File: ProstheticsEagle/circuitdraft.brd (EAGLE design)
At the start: 60 x 29.8 mm, 49 parts, among them IC1 BQ25887RGER, IC2 TPS54627DDAR, Q1 16 MHz

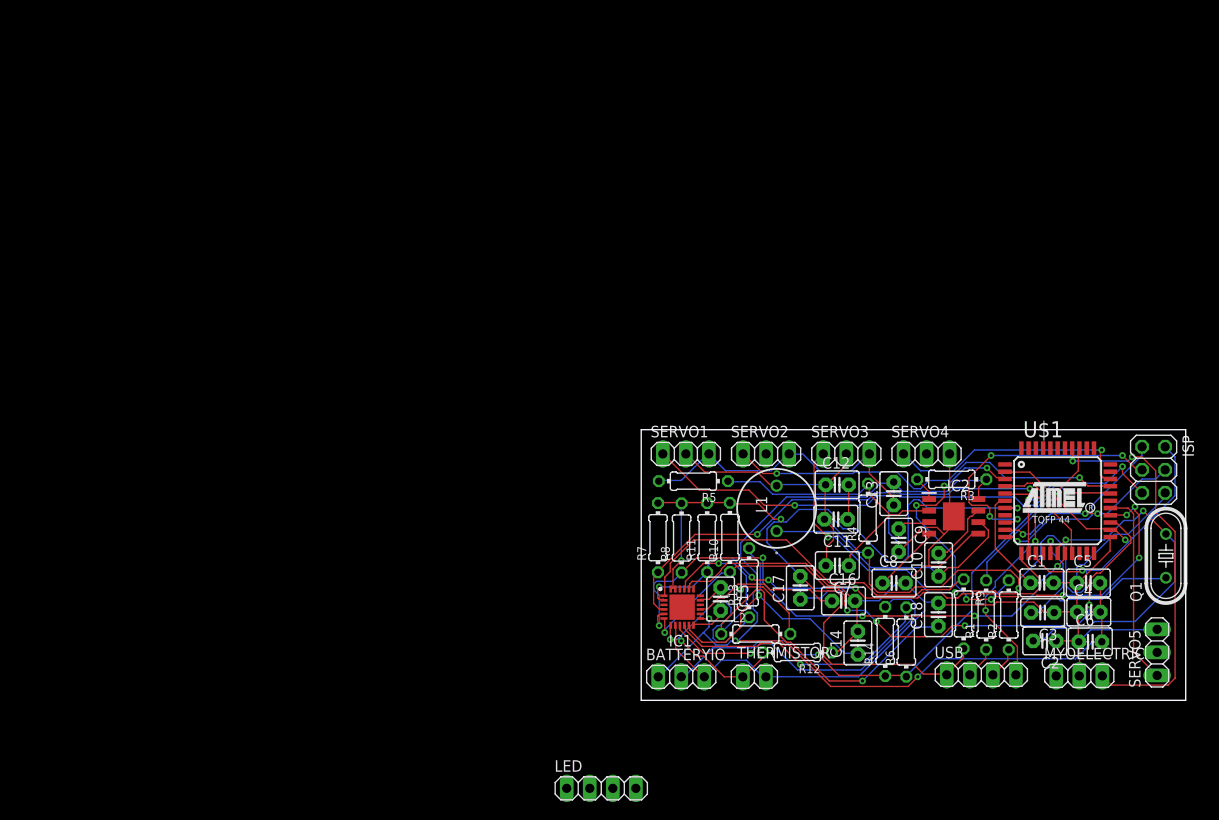
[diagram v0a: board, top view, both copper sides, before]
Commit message: Added surface mount parts
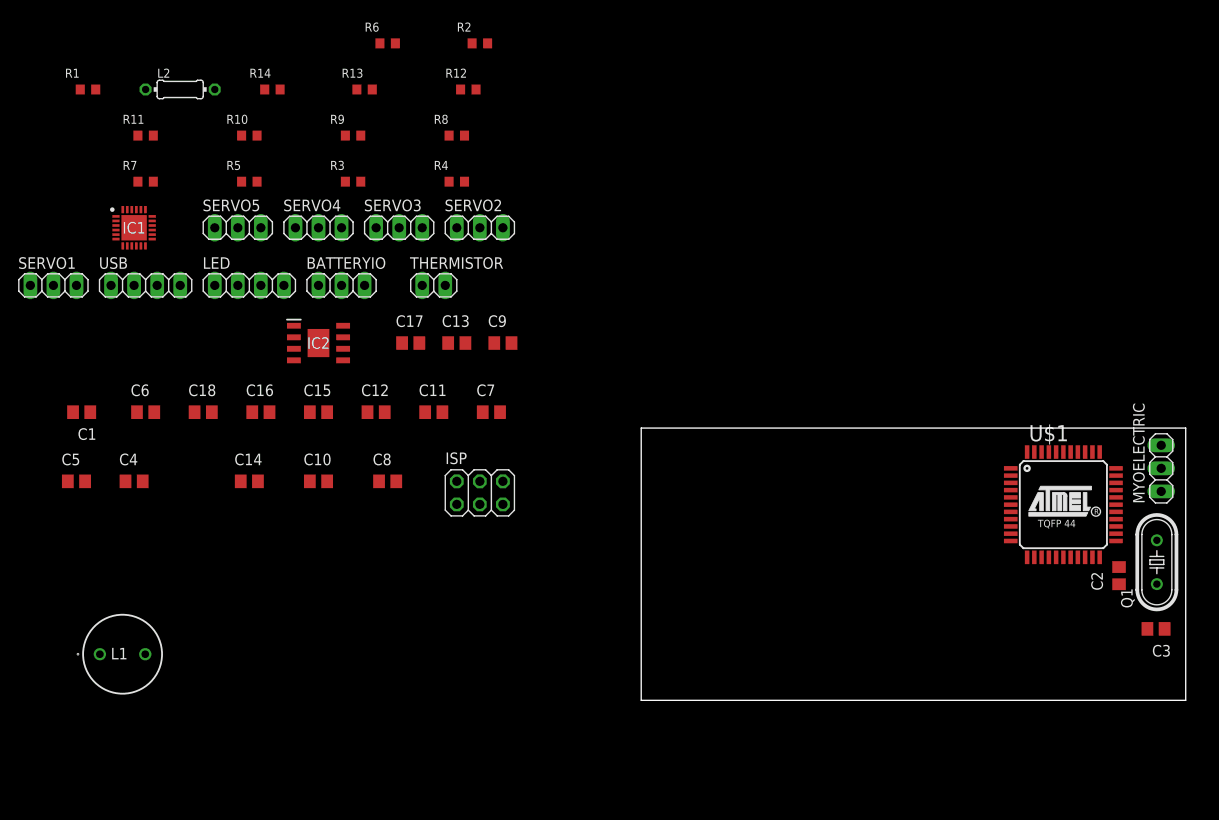
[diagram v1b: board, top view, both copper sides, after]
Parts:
- C1, C10, C11, C12, C13, C14, C15, C16, C17, C18, C2, C3, C4, C5, C6, C7, C8, C9: device capacitor-wima:C2.5-3 -> rcl:C0805
- R1, R10, R11, R12, R13, R14, R2, R3, R4, R5, R6, R7, R8, R9: device rcl:0204/7 -> rcl:R0603
- moved R1 114.7 mm to (-61.0, 67.3), turned to 0 degrees
- moved C5 112.1 mm to (-62.2, 24.1)
- moved SERVO5 111.6 mm to (-44.5, 52.1), turned to 0 degrees
- moved C1 107.5 mm to (-61.7, 31.8), turned to 180 degrees
- moved C6 107.1 mm to (-54.6, 31.8)
- moved C4 106.2 mm to (-55.9, 24.1)
- moved USB 101.6 mm to (-54.6, 45.7)
- moved R14 90.9 mm to (-40.6, 67.3), turned to 0 degrees
- moved L2 87.3 mm to (-50.8, 67.3)
- moved R6 87.3 mm to (-27.9, 72.4), turned to 0 degrees
- moved R2 85.8 mm to (-17.8, 72.4), turned to 0 degrees
- moved R9 85.5 mm to (-31.8, 62.2), turned to 0 degrees
- moved C18 84.0 mm to (-48.3, 31.8), turned to 0 degrees
- moved R11 76.1 mm to (-54.6, 62.2), turned to 0 degrees
- moved ISP 74.3 mm to (-17.8, 22.9), turned to 0 degrees
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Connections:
- removed net N$17: C11.1, C12.2
- removed net VOUT: MYOELECTRIC.1
- net AGND: now also C11.2, C12.2
- net POWER: now also C11.1, MYOELECTRIC.1; no longer C11.2
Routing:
- net AGND: track 216.7 -> 0.00 mm
- net POWER: track 121.4 -> 0.00 mm, vias 3 -> 0
- net B+: track 111.6 -> 0.00 mm, vias 3 -> 0
- net VBUS: track 101.7 -> 0.00 mm, vias 3 -> 0
- net INT: track 70.2 -> 0.00 mm, vias 5 -> 0
- net STAT: track 70.0 -> 0.00 mm, vias 8 -> 0
- net MIDDLE: track 61.5 -> 0.00 mm, vias 2 -> 0
- net SCL: track 61.1 -> 0.00 mm, vias 5 -> 0
- net SDA: track 59.1 -> 0.00 mm, vias 2 -> 0
- net SIGNAL1: track 53.8 -> 0.00 mm, vias 2 -> 0
- net N$21: track 51.7 -> 0.00 mm, vias 2 -> 0
- net SIGNAL2: track 44.5 -> 0.00 mm, vias 2 -> 0
- net N$12: track 43.9 -> 0.00 mm, vias 2 -> 0
- net SIGNAL3: track 41.3 -> 0.00 mm, vias 2 -> 0
- net N$7: track 40.5 -> 0.00 mm
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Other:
- board size 60 x 29.8 mm -> 60 x 30 mm

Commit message: fffff
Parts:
- removed BATTERYIO, MYOELECTRIC: (no value), pinhead:1X03
- removed THERMISTOR: (no value), pinhead:1X02
- added BATIO, MYO: (no value), pinhead:1X03
- added TS: (no value), pinhead:1X02
- LED: device pinhead:1X04 -> pinhead:1X03
- moved R7 112.0 mm to (48.9, 14.4)
- moved SERVO5 111.7 mm to (55.6, 2.57)
- moved R1 95.5 mm to (24.7, 25.0)
- moved R11 91.4 mm to (21.9, 12.1)
- moved C1 85.9 mm to (22.4, 14.2)
- moved R14 80.5 mm to (11.4, 5.91)
- moved R10 80.4 mm to (22.5, 15.9)
- moved L2 80.0 mm to (5.50, 10.4)
- moved C5 78.5 mm to (15.9, 16.4)
- moved R6 77.5 mm to (15.4, 8.09)
- moved IC1 77.0 mm to (11.0, 13.9), turned to 90 degrees
- moved R5 76.5 mm to (22.5, 18.1)
- moved R9 75.6 mm to (18.6, 5.93)
- moved C6 73.1 mm to (15.8, 12.2)
- moved C4 72.4 mm to (15.8, 14.3)
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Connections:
- removed net N$12: MYOELECTRIC.3, U$1.37
- removed net N$23: LED.4
- removed net N$24: LED.1
- new net DATAIN: LED.3
- new net MYOSIGNAL: MYO.3, U$1.37
- net AGND: now also BATIO.3, LED.2, MYO.2, TS.2; no longer BATTERYIO.3, LED.3, MYOELECTRIC.2, THERMISTOR.2
- net B+: now also BATIO.1; no longer BATTERYIO.1
- net MIDDLE: now also BATIO.2; no longer BATTERYIO.2
- net POWER: now also LED.1, MYO.1, SERVO2.2, SERVO4.2, SERVO5.2; no longer LED.2, MYOELECTRIC.1
- net TS: now also TS.1; no longer THERMISTOR.1
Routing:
- added copper zone on layer 1, net AGND
- added copper zone on layer 16, net AGND

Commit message: moved stuff
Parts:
- moved R10 3.32 mm to (25.8, 16.3)
- moved R6 0.41 mm to (15.8, 7.99)
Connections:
- net DATAIN: now also U$1.32
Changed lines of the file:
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@@
 </class>
 </classes>
-<designrules name="default">
-<description language="de">&lt;b&gt;EAGLE Design Rules&lt;/b&gt;
+<designrules name="jlcpcb2layer">
+<description language="en">&lt;b&gt;JLCPCB Design Rules by Jaap de Dood&lt;/b&gt;
 &lt;p&gt;
-Die Standard-Design-Rules sind so gewählt, dass sie für
-die meisten Anwendungen passen. Sollte ihre Platine
-besondere Anforderungen haben, treffen Sie die erforderlichen
-Einstellungen hier und speichern die Design Rules unter
-einem neuen Namen ab.</description>
-<description language="en">&lt;b&gt;EAGLE Design Rules&lt;/b&gt;
-&lt;p&gt;
-The default Design Rules have been set to cover
-a wide range of applications. Your particular design
-may have different requirements, so please make the
-necessary adjustments and save your customized
-design rules under a new name.</description>
+Please make sure your boards conform to these design rules.
+&lt;/p&gt;</description>
 <param name="layerSetup" value="(1*16)"/>
-<param name="mtCopper" value="0.035mm 0.035mm 0.035mm 0.035mm 0.035mm 0.035mm 0.035mm 0.035mm 0.035mm 0.035mm 0.035mm 0.035mm 0.035mm 0.035mm 0.035mm 0.035mm"/>
-<param name="mtIsolate" value="1.5mm 0.15mm 0.2mm 0.15mm 0.2mm 0.15mm 0.2mm 0.15mm 0.2mm 0.15mm 0.2mm 0.15mm 0.2mm 0.15mm 0.2mm"/>
-<param name="mdWireWire" value="6mil"/>
-<param name="mdWirePad" value="6mil"/>
-<param name="mdWireVia" value="6mil"/>
-<param name="mdPadPad" value="6mil"/>
-<param name="mdPadVia" value="6mil"/>
-<param name="mdViaVia" value="6mil"/>
-<param name="mdSmdPad" value="6mil"/>
-<param name="mdSmdVia" value="6mil"/>
-<param name="mdSmdSmd" value="6mil"/>
-<param name="mdViaViaSameLayer" value="6mil"/>
+<param name="mtCopper" value="0.035559375mm 0.0356mm 0.0356mm 0.0356mm 0.0356mm 0.0356mm 0.0356mm 0.0356mm 0.0356mm 0.0356mm 0.0356mm 0.0356mm 0.0356mm 0.0356mm 0.0356mm 0.035559375mm"/>
+<param name="mtIsolate" value="1.6mm 0.1499mm 0.2007mm 0.1499mm 0.2007mm 0.1499mm 0.2007mm 0.1499mm 0.2007mm 0.1499mm 0.2007mm 0.1499mm 0.2007mm 0.1499mm 0.2007mm"/>
+<param name="mdWireWire" value="5mil"/>
+<param name="mdWirePad" value="5mil"/>
+<param name="mdWireVia" value="5mil"/>
+<param name="mdPadPad" value="5mil"/>
+<param name="mdPadVia" value="5mil"/>
+<param name="mdViaVia" value="5mil"/>
+<param name="mdSmdPad" value="5mil"/>
+<param name="mdSmdVia" value="5mil"/>
+<param name="mdSmdSmd" value="5mil"/>
+<param name="mdViaViaSameLayer" value="8mil"/>
 <param name="mnLayersViaInSmd" value="2"/>
-<param name="mdCopperDimension" value="40mil"/>
+<param name="mdCopperDimension" value="8mil"/>
 <param name="mdDrill" value="6mil"/>
 <param name="mdSmdStop" value="0mil"/>
-<param name="msWidth" value="6mil"/>
-<param name="msDrill" value="0.35mm"/>
-<param name="msMicroVia" value="9.99mm"/>
+<param name="msWidth" value="5mil"/>
+<param name="msDrill" value="12mil"/>
+<param name="msMicroVia" value="12mil"/>
 <param name="msBlindViaRatio" value="0.5"/>
 <param name="rvPadTop" value="0.25"/>
@@
 <param name="rvMicroViaOuter" value="0.25"/>
 <param name="rvMicroViaInner" value="0.25"/>
-<param name="rlMinPadTop" value="10mil"/>
+<param name="rlMinPadTop" value="5mil"/>
 <param name="rlMaxPadTop" value="20mil"/>
-<param name="rlMinPadInner" value="10mil"/>
+<param name="rlMinPadInner" value="5mil"/>
 <param name="rlMaxPadInner" value="20mil"/>
-<param name="rlMinPadBottom" value="10mil"/>
+<param name="rlMinPadBottom" value="5mil"/>
 <param name="rlMaxPadBottom" value="20mil"/>
-<param name="rlMinViaOuter" value="8mil"/>
+<param name="rlMinViaOuter" value="3mil"/>
 <param name="rlMaxViaOuter" value="20mil"/>
-<param name="rlMinViaInner" value="8mil"/>
+<param name="rlMinViaInner" value="3mil"/>
 <param name="rlMaxViaInner" value="20mil"/>
-<param name="rlMinMicroViaOuter" value="4mil"/>
+<param name="rlMinMicroViaOuter" value="3mil"/>
 <param name="rlMaxMicroViaOuter" value="20mil"/>
-<param name="rlMinMicroViaInner" value="4mil"/>
+<param name="rlMinMicroViaInner" value="3mil"/>
 <param name="rlMaxMicroViaInner" value="20mil"/>
 <param name="psTop" value="-1"/>
@@
 <param name="mvStopFrame" value="1"/>
 <param name="mvCreamFrame" value="0"/>
-<param name="mlMinStopFrame" value="4mil"/>
-<param name="mlMaxStopFrame" value="4mil"/>
+<param name="mlMinStopFrame" value="2.5mil"/>
+<param name="mlMaxStopFrame" value="2.5mil"/>
 <param name="mlMinCreamFrame" value="0mil"/>
 <param name="mlMaxCreamFrame" value="0mil"/>
@@
 <attribute name="SPICEPREFIX" value="R" x="85.66" y="-42.31" size="1.778" layer="27" display="off"/>
 </element>
-<element name="R10" library="rcl" library_urn="urn:adsk.eagle:library:334" package="R0603" package3d_urn="urn:adsk.eagle:package:23555/3" value="10000 Ohms" x="22.5" y="15.9" smashed="yes">
-<attribute name="NAME" x="24.36" y="15.3954" size="0.9906" layer="25" ratio="10"/>
-<attribute name="POPULARITY" value="77" x="65.68" y="-46.33" size="1.778" layer="27" display="off"/>
-<attribute name="SPICEPREFIX" value="R" x="65.68" y="-46.33" size="1.778" layer="27" display="off"/>
+<element name="R10" library="rcl" library_urn="urn:adsk.eagle:library:334" package="R0603" package3d_urn="urn:adsk.eagle:package:23555/3" value="10000 Ohms" x="25.8" y="16.3" smashed="yes">
+<attribute name="NAME" x="27.66" y="15.7954" size="0.9906" layer="25" ratio="10"/>
+<attribute name="POPULARITY" value="77" x="68.98" y="-45.93" size="1.778" layer="27" display="off"/>
+<attribute name="SPICEPREFIX" value="R" x="68.98" y="-45.93" size="1.778" layer="27" display="off"/>
 </element>
 <element name="R11" library="rcl" library_urn="urn:adsk.eagle:library:334" package="R0603" package3d_urn="urn:adsk.eagle:package:23555/3" value="10000 Ohms" x="21.89" y="12.13" smashed="yes">
@@
 <attribute name="SPICEPREFIX" value="R" x="65.7" y="-39.1" size="1.778" layer="27" display="off"/>
 </element>
-<element name="R6" library="rcl" library_urn="urn:adsk.eagle:library:334" package="R0603" package3d_urn="urn:adsk.eagle:package:23555/3" value="12 Ohms" x="15.36" y="8.09" smashed="yes">
-<attribute name="NAME" x="12.82" y="9.3854" size="0.9906" layer="25" ratio="10"/>
-<attribute name="POPULARITY" value="77" x="43.3" y="-64.3" size="1.778" layer="27" display="off"/>
-<attribute name="SPICEPREFIX" value="R" x="43.3" y="-64.3" size="1.778" layer="27" display="off"/>
+<element name="R6" library="rcl" library_urn="urn:adsk.eagle:library:334" package="R0603" package3d_urn="urn:adsk.eagle:package:23555/3" value="12 Ohms" x="15.76" y="7.99" smashed="yes">
+<attribute name="NAME" x="13.22" y="9.2854" size="0.9906" layer="25" ratio="10"/>
+<attribute name="POPULARITY" value="77" x="43.7" y="-64.4" size="1.778" layer="27" display="off"/>
+<attribute name="SPICEPREFIX" value="R" x="43.7" y="-64.4" size="1.778" layer="27" display="off"/>
 </element>
 <element name="R7" library="rcl" library_urn="urn:adsk.eagle:library:334" package="R0603" package3d_urn="urn:adsk.eagle:package:23555/3" value="10000 Ohms" x="48.89" y="14.45" smashed="yes">
@@
 <wire x1="20.97" y1="4.67" x2="39.95" y2="21.67" width="0" layer="19" extent="1-1"/>
 <wire x1="19.5" y1="5.93" x2="20.97" y2="4.67" width="0" layer="19" extent="1-1"/>
-<wire x1="23.35" y1="15.9" x2="19.5" y2="5.93" width="0" layer="19" extent="1-1"/>
-<wire x1="22.74" y1="12.13" x2="23.35" y2="15.9" width="0" layer="19" extent="1-1"/>
+<wire x1="26.65" y1="16.3" x2="19.5" y2="5.93" width="0" layer="19" extent="1-1"/>
+<wire x1="22.74" y1="12.13" x2="26.65" y2="16.3" width="0" layer="19" extent="1-1"/>
 <wire x1="49.74" y1="14.45" x2="22.74" y2="12.13" width="0" layer="19" extent="1-1"/>
 <wire x1="9.03" y1="13.17" x2="49.74" y2="14.45" width="0" layer="19" extent="1-1"/>
@@
 <wire x1="2.68" y1="15.58" x2="50.22" y2="28.16" width="0" layer="19" extent="1-1"/>
 <wire x1="10.51" y1="5.91" x2="2.68" y2="15.58" width="0" layer="19" extent="1-1"/>
-<wire x1="14.51" y1="8.09" x2="10.51" y2="5.91" width="0" layer="19" extent="1-1"/>
+<wire x1="14.91" y1="7.99" x2="10.51" y2="5.91" width="0" layer="19" extent="1-1"/>
 </signal>
 <signal name="SCL">
@@
 <contactref element="IC1" pad="10"/>
 <contactref element="R6" pad="2"/>
-<wire x1="13.03" y1="14.17" x2="16.21" y2="8.09" width="0" layer="19" extent="1-1"/>
+<wire x1="13.03" y1="14.17" x2="16.61" y2="7.99" width="0" layer="19" extent="1-1"/>
 </signal>
 <signal name="N$7">
@@
 <contactref element="R10" pad="1"/>
 <contactref element="U$1" pad="25"/>
-<wire x1="21.65" y1="15.9" x2="53.62" y2="19.96" width="0" layer="19" extent="1-1"/>
-<wire x1="12.28" y1="11.92" x2="21.65" y2="15.9" width="0" layer="19" extent="1-1"/>
+<wire x1="24.95" y1="16.3" x2="53.62" y2="19.96" width="0" layer="19" extent="1-1"/>
+<wire x1="12.28" y1="11.92" x2="24.95" y2="16.3" width="0" layer="19" extent="1-1"/>
 </signal>
 <signal name="STAT">
@@
 <signal name="DATAIN">
 <contactref element="LED" pad="3"/>
+<contactref element="U$1" pad="32"/>
+<wire x1="16.04" y1="2.6" x2="53.62" y2="25.56" width="0" layer="19" extent="1-1"/>
 </signal>
 <signal name="MYOSIGNAL">
